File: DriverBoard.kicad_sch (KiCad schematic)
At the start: 0 parts

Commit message: 原理图:完成接口部分
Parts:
- added J1, J2: Conn_02x06_Odd_Even, symbol Connector_Generic:Conn_02x06_Odd_Even
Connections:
- new net +3.3V: J2.9 (Pin_9)
- new net +5V: J2.7 (Pin_7)
- new net ADC1_BusCurr: J1.9 (Pin_9)
- new net ADC1_BusVol: J1.7 (Pin_7)
- new net ADC1_U: J1.1 (Pin_1)
- new net ADC1_V: J1.3 (Pin_3)
- new net ADC1_W: J1.5 (Pin_5)
- new net ADC2_U: J2.1 (Pin_1)
- new net ADC2_V: J2.3 (Pin_3)
- new net ADC2_W: J2.5 (Pin_5)
- new net GND: J1.11 (Pin_11), J2.11 (Pin_11)
- new net PWM1_CH1: J1.2 (Pin_2)
- new net PWM1_CH1N: J1.4 (Pin_4)
- new net PWM1_CH2: J1.6 (Pin_6)
- new net PWM1_CH2N: J1.8 (Pin_8)
- new net PWM1_CH3: J1.10 (Pin_10)
- new net PWM1_CH3N: J1.12 (Pin_12)
- new net PWM8_CH1: J2.2 (Pin_2)
- new net PWM8_CH1N: J2.4 (Pin_4)
- new net PWM8_CH2: J2.6 (Pin_6)
- new net PWM8_CH2N: J2.8 (Pin_8)
- new net PWM8_CH3: J2.10 (Pin_10)
- new net PWM8_CH3N: J2.12 (Pin_12)
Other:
- added sheet PowerInput (Power.kicad_sch)
- added sheet Pre_Driver (Pre_Driver.kicad_sch)
- added sheet ThreePhase (ThreePhase.kicad_sch)
- added sheet YunFang (YunFang.kicad_sch)

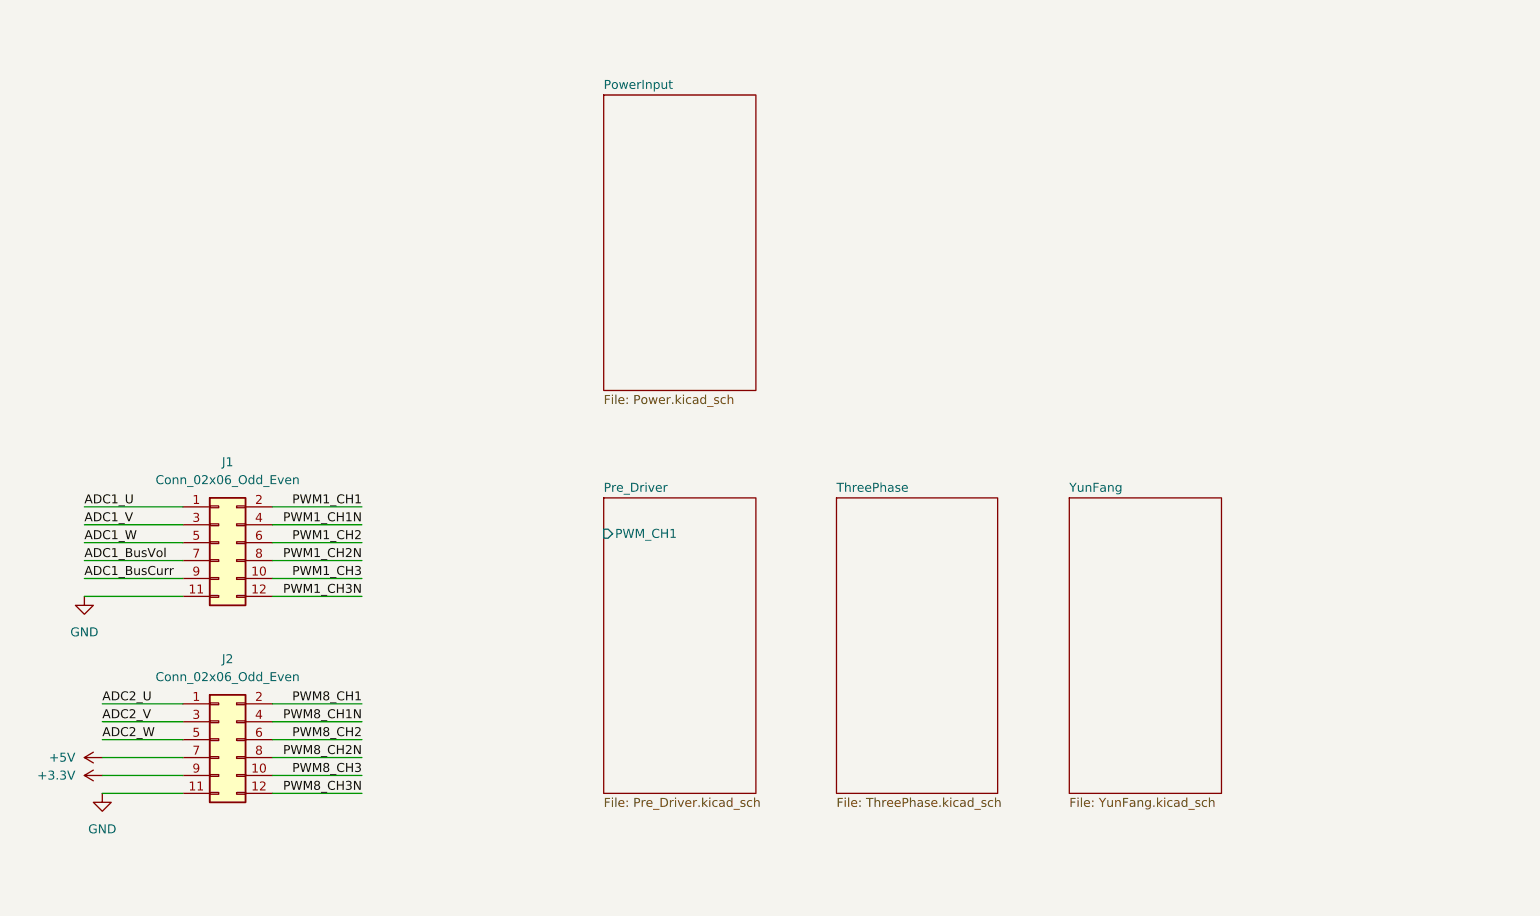
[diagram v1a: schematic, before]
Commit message: 增加部分接口
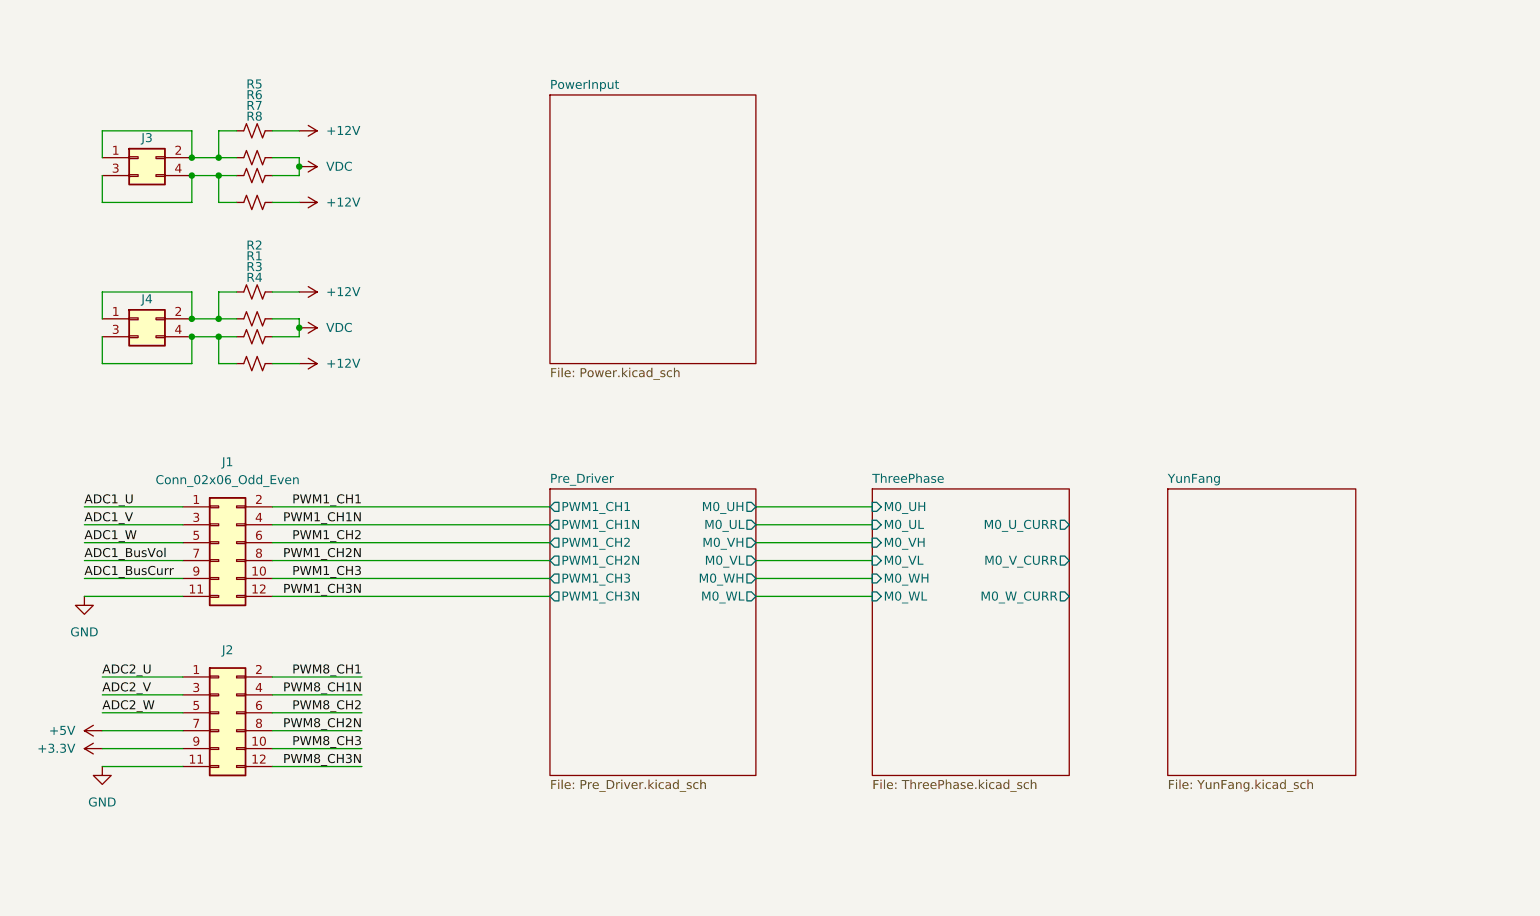
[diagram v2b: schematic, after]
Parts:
- added J3, J4: Conn_02x02_Odd_Even, symbol Connector_Generic:Conn_02x02_Odd_Even
- added R1, R2, R3, R4, R5, R6, R7, R8: R_Small_US, symbol Device:R_Small_US
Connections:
- new net: J3.3 (Pin_3), J3.4 (Pin_4), R7.1, R8.1
- new net: J4.3 (Pin_3), J4.4 (Pin_4), R3.1, R4.1
- new net: J3.1 (Pin_1), J3.2 (Pin_2), R5.1, R6.1
- new net: J4.1 (Pin_1), J4.2 (Pin_2), R1.1, R2.1
- new net +12V: R2.2, R4.2, R5.2, R8.2
- new net VDC: R1.2, R3.2, R6.2, R7.2
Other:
- sheet Pre_Driver ports: added M0_UH, M0_UL, M0_VH, M0_VL, M0_WH, M0_WL, PWM1_CH1, PWM1_CH1N, PWM1_CH2, PWM1_CH2N, PWM1_CH3, PWM1_CH3N; removed PWM_CH1
- sheet ThreePhase ports: added M0_UH, M0_UL, M0_U_CURR, M0_VH, M0_VL, M0_V_CURR, M0_WH, M0_WL, M0_W_CURR; removed none
- moved on the sheet: J2

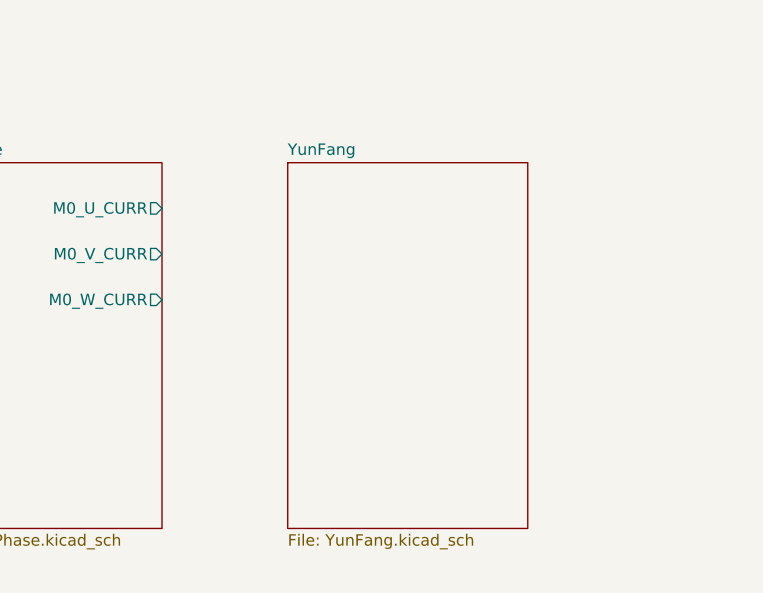
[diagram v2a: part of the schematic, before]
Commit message: 增加预驱/三相桥电路
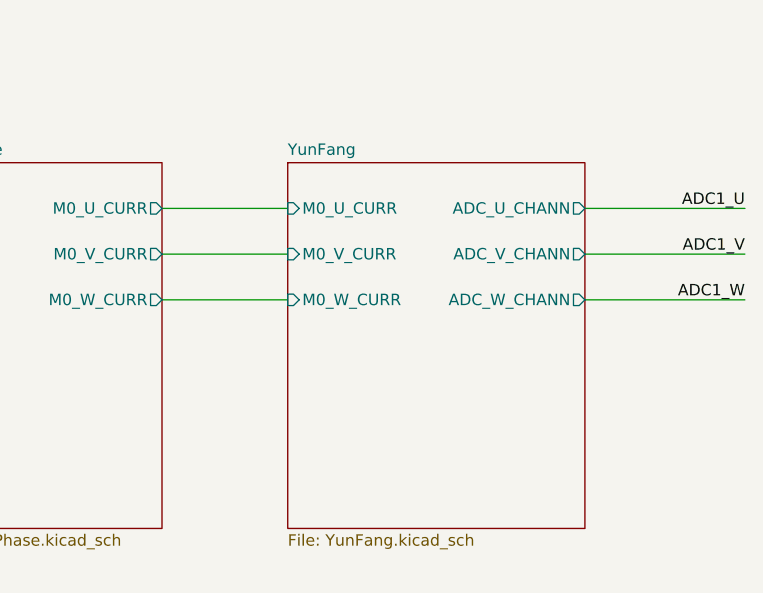
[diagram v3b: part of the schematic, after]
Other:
- sheet YunFang ports: added ADC_U_CHANN, ADC_V_CHANN, ADC_W_CHANN, M0_U_CURR, M0_V_CURR, M0_W_CURR; removed none

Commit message: 优化5V电源/预驱电路/三相桥/运放
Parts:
- removed J3, J4: Conn_02x02_Odd_Even, symbol Connector_Generic:Conn_02x02_Odd_Even
- removed R1, R2, R3, R4, R5, R6, R7, R8: R_Small_US, symbol Device:R_Small_US
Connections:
- net ADC1_BusVol renamed BusVoltage
- net PWM1_CH1 renamed Pre_Driver/U1_IN_H
- net PWM1_CH1N renamed Pre_Driver/U1_IN_L
- net PWM1_CH2 renamed Pre_Driver/V1_IN_H
- net PWM1_CH2N renamed Pre_Driver/V1_IN_L
- net PWM1_CH3 renamed Pre_Driver/W1_IN_H
- net PWM1_CH3N renamed Pre_Driver/W1_IN_L
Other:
- sheet PowerInput ports: added BUS_VOLTAGE; removed none
- sheet Pre_Driver ports: added U1, U1_IN_H, U1_IN_L, U1_OUT_H, U1_OUT_L, V1, V1_IN_H, V1_IN_L, V1_OUT_H, V1_OUT_L, W1, W1_IN_H, W1_IN_L, W1_OUT_H, W1_OUT_L; removed M0_UH, M0_UL, M0_VH, M0_VL, M0_WH, M0_WL, PWM1_CH1, PWM1_CH1N, PWM1_CH2, PWM1_CH2N, PWM1_CH3, PWM1_CH3N
- sheet ThreePhase ports: added U1, U1_CURR, U1_H, U1_L, V1, V1_CURR, V1_H, V1_L, W1, W1_CURR, W1_H, W1_L; removed M0_UH, M0_UL, M0_U_CURR, M0_VH, M0_VL, M0_V_CURR, M0_WH, M0_WL, M0_W_CURR
- sheet YunFang ports: added U1_AMP, U1_CURR, V1_AMP, V1_CURR, W1_AMP, W1_CURR; removed ADC_U_CHANN, ADC_V_CHANN, ADC_W_CHANN, M0_U_CURR, M0_V_CURR, M0_W_CURR

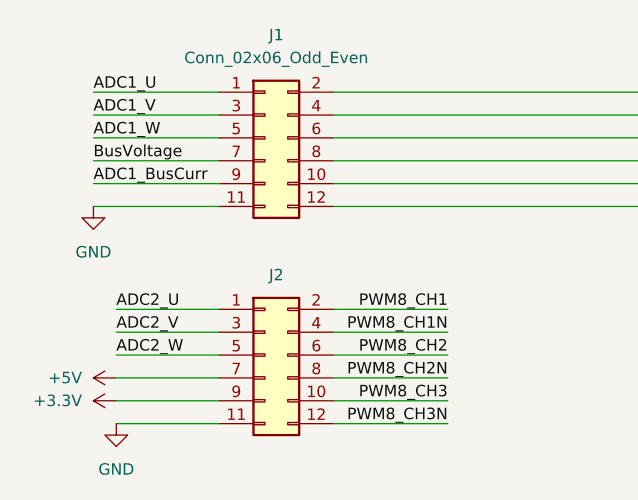
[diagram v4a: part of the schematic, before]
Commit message: 分配部分封装
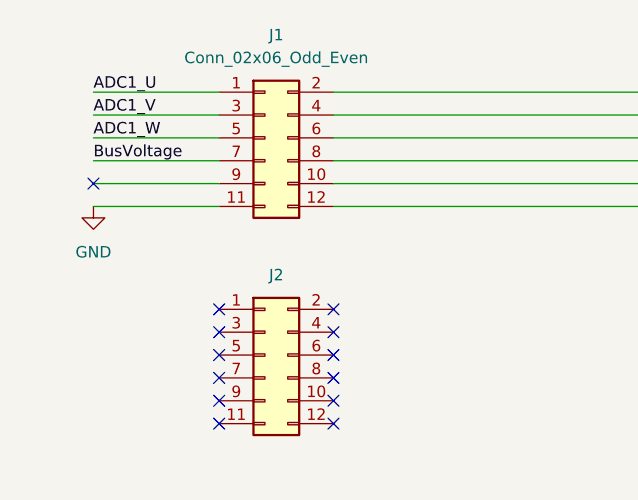
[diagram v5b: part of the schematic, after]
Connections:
- net GND: no longer J2.11 (Pin_11)
- net +3.3V: no longer names the net of J2.9 (Pin_9)
- net +5V: no longer names the net of J2.7 (Pin_7)
- net ADC1_BusCurr: no longer names the net of J1.9 (Pin_9)
- net ADC2_U: no longer names the net of J2.1 (Pin_1)
- net ADC2_V: no longer names the net of J2.3 (Pin_3)
- net ADC2_W: no longer names the net of J2.5 (Pin_5)
- net PWM8_CH1: no longer names the net of J2.2 (Pin_2)
- net PWM8_CH1N: no longer names the net of J2.4 (Pin_4)
- net PWM8_CH2: no longer names the net of J2.6 (Pin_6)
- net PWM8_CH2N: no longer names the net of J2.8 (Pin_8)
- net PWM8_CH3: no longer names the net of J2.10 (Pin_10)
- net PWM8_CH3N: no longer names the net of J2.12 (Pin_12)
- no-connect marks 0 -> 13

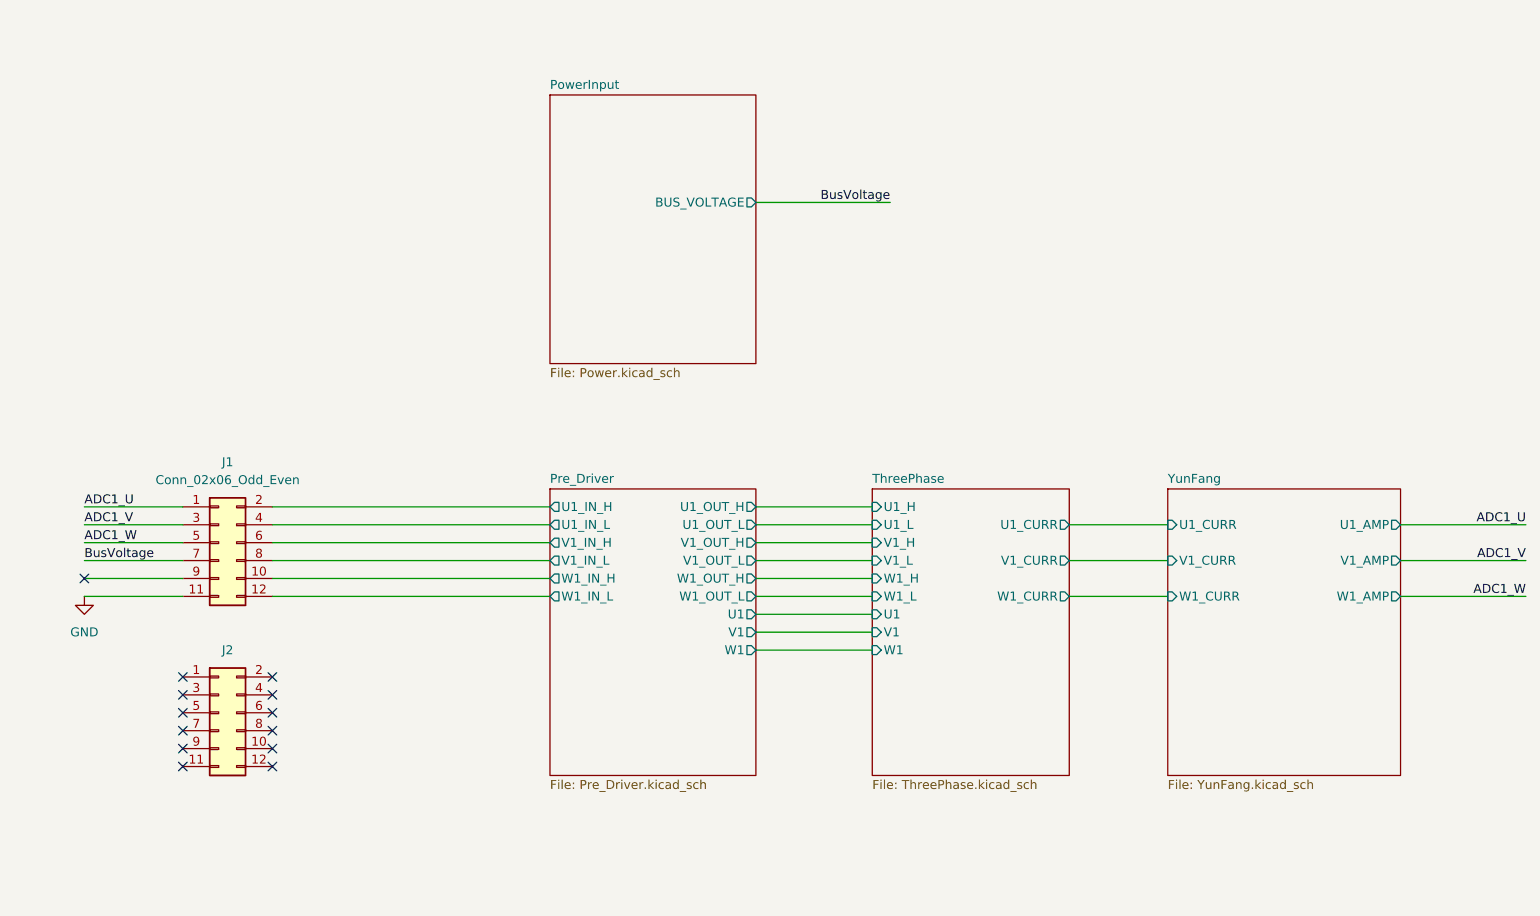
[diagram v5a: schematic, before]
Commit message: 生成网表并添加到PCB
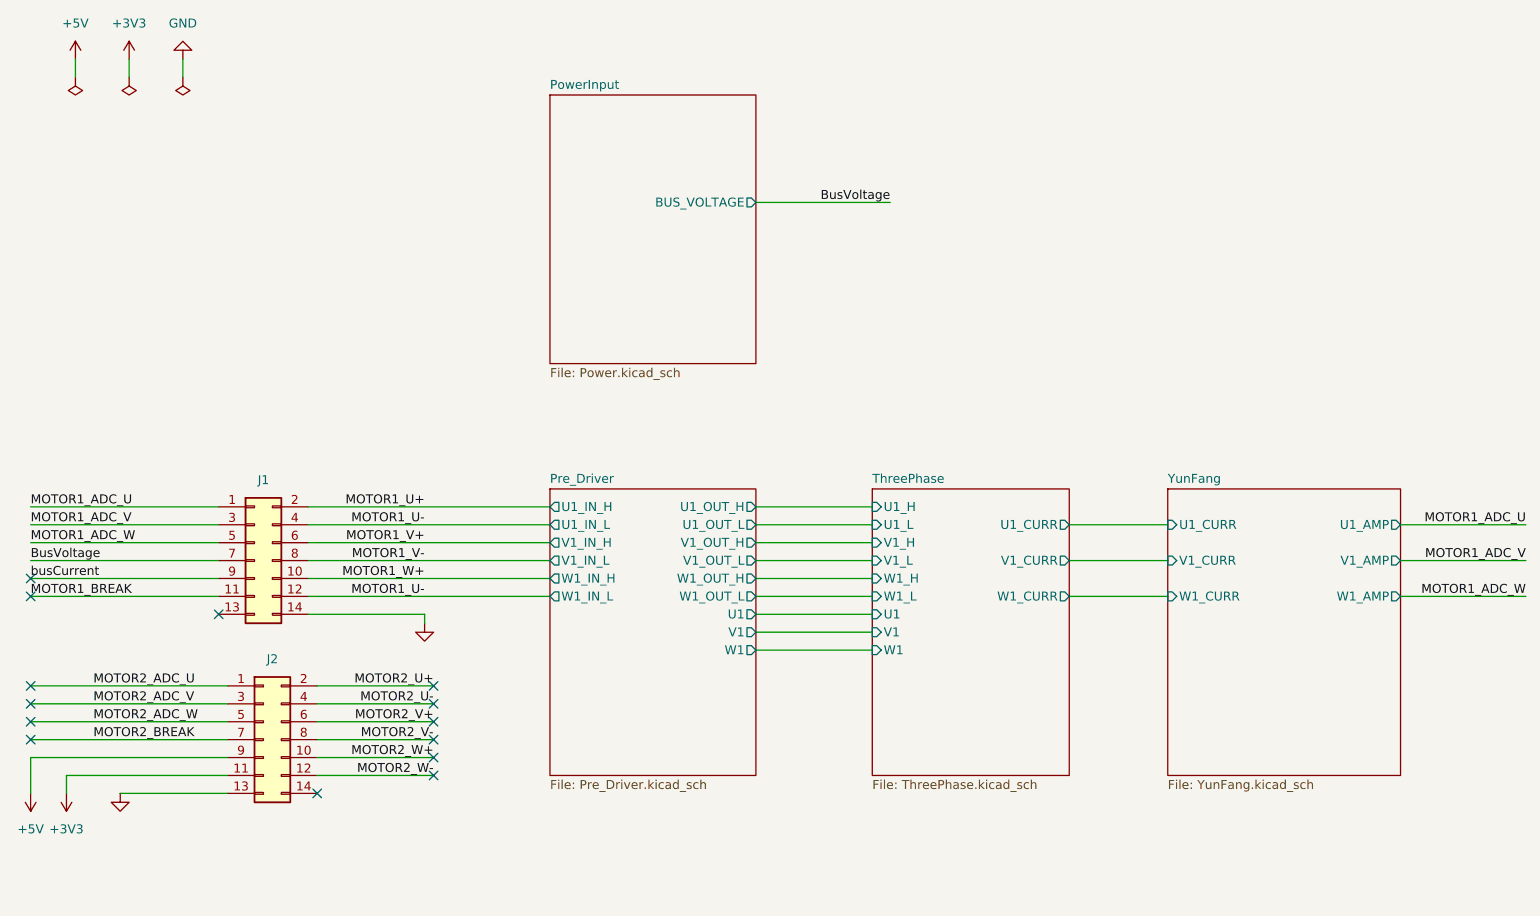
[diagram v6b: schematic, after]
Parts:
- removed J1, J2: Conn_02x06_Odd_Even, symbol Connector_Generic:Conn_02x06_Odd_Even
- added J1, J2: Conn_02x07_Odd_Even, Connector_PinSocket_1.27mm:PinSocket_2x07_P1.27mm_Vertical_SMD, symbol Connector_Generic:Conn_02x07_Odd_Even
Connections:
- net BusVoltage: now also J1.7 (Pin_7)
- net GND: now also J1.14 (Pin_14), J2.13 (Pin_13)
- new net +3V3: J2.11 (Pin_11)
- new net +5V: J2.9 (Pin_9)
- new net MOTOR1_ADC_U: J1.1 (Pin_1)
- new net MOTOR1_ADC_V: J1.3 (Pin_3)
- new net MOTOR1_ADC_W: J1.5 (Pin_5)
- new net MOTOR1_BREAK: J1.11 (Pin_11)
- new net MOTOR1_U+: J1.2 (Pin_2)
- new net MOTOR1_U-: J1.12 (Pin_12), J1.4 (Pin_4)
- new net MOTOR1_V+: J1.6 (Pin_6)
- new net MOTOR1_V-: J1.8 (Pin_8)
- new net MOTOR1_W+: J1.10 (Pin_10)
- new net MOTOR2_ADC_U: J2.1 (Pin_1)
- new net MOTOR2_ADC_V: J2.3 (Pin_3)
- new net MOTOR2_ADC_W: J2.5 (Pin_5)
- new net MOTOR2_BREAK: J2.7 (Pin_7)
- new net MOTOR2_U+: J2.2 (Pin_2)
- new net MOTOR2_U-: J2.4 (Pin_4)
- new net MOTOR2_V+: J2.6 (Pin_6)
- new net MOTOR2_V-: J2.8 (Pin_8)
- new net MOTOR2_W+: J2.10 (Pin_10)
- new net MOTOR2_W-: J2.12 (Pin_12)
- new net busCurrent: J1.9 (Pin_9)
- no-connect marks 13 -> 14

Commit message: 原理图增加motor2部分
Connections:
- no-connect marks 14 -> 5
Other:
- sheet Pre_Driver ports: added U2, U2_IN_H, U2_IN_L, U2_OUT_H, U2_OUT_L, V2, V2_IN_H, V2_IN_L, V2_OUT_H, V2_OUT_L, W2, W2_IN_H, W2_IN_L, W2_OUT_H, W2_OUT_L; removed none
- sheet ThreePhase ports: added U2, U2_CURR, U2_H, U2_L, V2, V2_CURR, V2_H, V2_L, W2, W2_CURR, W2_H, W2_L; removed none
- sheet YunFang ports: added U2_AMP, U2_CURR, V2_AMP, V2_CURR, W2_AMP, W2_CURR; removed none
